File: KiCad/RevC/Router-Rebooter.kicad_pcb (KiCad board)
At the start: 2 copper layers, 62 x 49 mm, 18 parts, among them J1 12V Out, J3 12V In, K1 OMRON G5LE-1-VD, Q1 PN2222A, U1 PSU2-5, U2 ESP32-C3-Zero

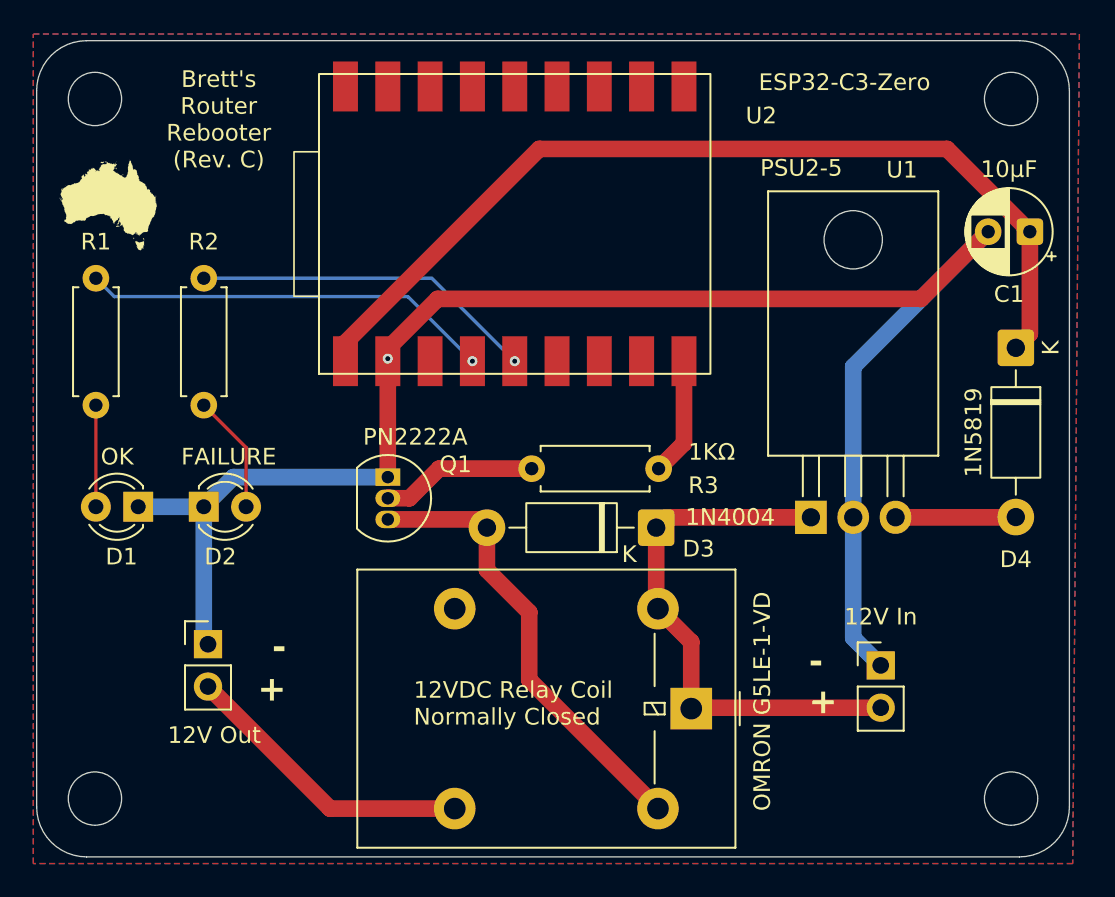
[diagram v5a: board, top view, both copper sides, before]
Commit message: Moved LED resistors to fix USB-C access to ESP32
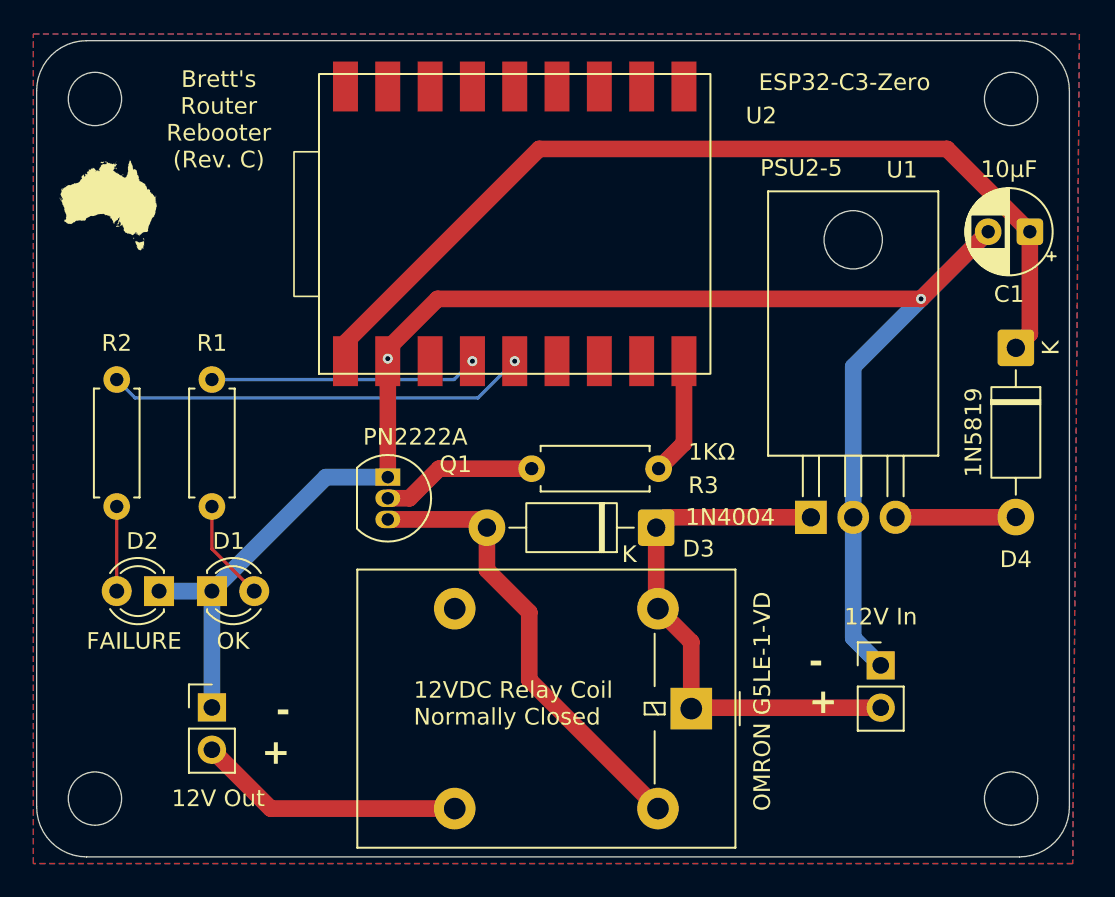
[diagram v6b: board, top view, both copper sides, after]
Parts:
- moved R1 9.25 mm to (67.8, 52.9)
- moved R2 8.02 mm to (62.1, 52.9)
- moved D1 6.73 mm to (67.8, 65.6), turned to 0 degrees
- moved D2 5.73 mm to (64.6, 65.6), turned to 180 degrees
- moved J1 3.80 mm to (67.8, 72.6)
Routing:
- net Net-(U2-IO0): track 24.7 -> 16.1 mm
- net Net-(U2-IO1): track 20.7 -> 25.3 mm
- net Net-(D2-A): track 7.15 -> 5.08 mm
- net /+12V_{OUT}: track 17.8 -> 16.0 mm
- net GND: track 100.8 -> 100.3 mm, vias 1 -> 2
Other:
- board text added: "Brett Hallen, Apr 2026"
- board text removed: "Brett Hallen, Mar 2026"
- board text removed: "USB Power Bypass Open: ESP32 powered via USB Closed: ESP32 powered via 12V input"
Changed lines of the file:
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@@
 	(title_block
 		(title "Broadband Router Rebooter")
-		(date "28/MAR/2026")
+		(date "30/APR/2026")
 		(rev "C")
 		(company "Brett Hallen")
@@
 	(footprint "Resistor_THT:R_Axial_DIN0207_L6.3mm_D2.5mm_P7.62mm_Horizontal"
 		(layer "F.Cu")
-		(at 60.8064 46.8524 -90)
+		(at 67.7734 52.9334 -90)
 		(descr "Resistor, Axial_DIN0207 series, Axial, Horizontal, pin pitch=7.62mm, 0.25W = 1/4W, length*diameter=6.3*2.5mm^2, http://cdn-reichelt.de/documents/datenblatt/B400/1_4W%23YAG.pdf")
 		(tags "Resistor Axial_DIN0207 series Axial Horizontal pin pitch 7.62mm 0.25W = 1/4W length 6.3mm diameter 2.5mm")
@@
 	(footprint "Connector_PinHeader_2.54mm:PinHeader_1x02_P2.54mm_Vertical"
 		(layer "F.Cu")
-		(at 67.5374 68.8234)
+		(at 67.7734 72.6184)
 		(descr "Through hole straight pin header, 1x02, 2.54mm pitch, single row")
 		(tags "Through hole pin header THT 1x02 2.54mm single row")
@@
 	(footprint "LED_THT:LED_D3.0mm"
 		(layer "F.Cu")
-		(at 67.2834 60.5684)
+		(at 64.5984 65.6334 180)
 		(descr "LED, diameter 3.0mm, 2 pins, generated by kicad-footprint-generator")
 		(tags "LED")
@@
 		)
 		(property "Sim.Pins" "1=K 2=A"
-			(at 0 0 0)
+			(at 0 0 180)
 			(unlocked yes)
 			(layer "F.Fab")
@@
 		(attr through_hole)
 		(fp_line
-			(start -0.29 -1.236)
-			(end -0.29 -1.08)
+			(start -0.29 1.08)
+			(end -0.29 1.236)
 			(stroke
 				(width 0.12)
@@
 		)
 		(fp_line
-			(start -0.29 1.08)
-			(end -0.29 1.236)
+			(start -0.29 -1.236)
+			(end -0.29 -1.08)
 			(stroke
 				(width 0.12)
@@
 		)
 		(fp_arc
-			(start -0.29 -1.235516)
-			(mid 1.36566 -1.987699)
-			(end 2.941437 -1.08)
+			(start 2.941437 1.08)
+			(mid 1.36566 1.987699)
+			(end -0.29 1.235516)
 			(stroke
 				(width 0.12)
@@
 		)
 		(fp_arc
-			(start 0.229039 -1.08)
-			(mid 1.27 -1.5)
-			(end 2.310961 -1.08)
+			(start 2.310961 1.08)
+			(mid 1.27 1.5)
+			(end 0.229039 1.08)
 			(stroke
 				(width 0.12)
@@
 		)
 		(fp_arc
-			(start 2.310961 1.08)
-			(mid 1.27 1.5)
-			(end 0.229039 1.08)
+			(start 0.229039 -1.08)
+			(mid 1.27 -1.5)
+			(end 2.310961 -1.08)
 			(stroke
 				(width 0.12)
@@
 		)
 		(fp_arc
-			(start 2.941437 1.08)
-			(mid 1.36566 1.987699)
-			(end -0.29 1.235516)
+			(start -0.29 -1.235516)
+			(mid 1.36566 -1.987699)
+			(end 2.941437 -1.08)
 			(stroke
 				(width 0.12)
@@
 		)
 		(fp_line
-			(start -1.15 -2.21)
-			(end -1.15 2.21)
+			(start 3.69 2.21)
+			(end 3.69 -2.21)
 			(stroke
 				(width 0.05)
@@
 		)
 		(fp_line
-			(start -1.15 2.21)
-			(end 3.69 2.21)
+			(start 3.69 -2.21)
+			(end -1.15 -2.21)
 			(stroke
 				(width 0.05)
@@
 		)
 		(fp_line
-			(start 3.69 -2.21)
-			(end -1.15 -2.21)
+			(start -1.15 2.21)
+			(end 3.69 2.21)
 			(stroke
 				(width 0.05)
@@
 		)
 		(fp_line
-			(start 3.69 2.21)
-			(end 3.69 -2.21)
+			(start -1.15 -2.21)
+			(end -1.15 2.21)
 			(stroke
 				(width 0.05)
@@
 		)
 		(pad "1" thru_hole rect
-			(at 0 0)
+			(at 0 0 180)
 			(size 1.8 1.8)
 			(drill 0.9)
@@
 		)
 		(pad "2" thru_hole circle
-			(at 2.54 0)
+			(at 2.54 0 180)
 			(size 1.8 1.8)
 			(drill 0.9)
@@
 	(footprint "LED_THT:LED_D3.0mm"
 		(layer "F.Cu")
-		(at 63.3464 60.5684 180)
+		(at 67.7734 65.6334)
 		(descr "LED, diameter 3.0mm, 2 pins, generated by kicad-footprint-generator")
 		(tags "LED")
@@
 		)
 		(property "Sim.Pins" "1=K 2=A"
-			(at 0 0 180)
+			(at 0 0 0)
 			(unlocked yes)
 			(layer "F.Fab")
@@
 		(attr through_hole)
 		(fp_line
-			(start -0.29 1.08)
-			(end -0.29 1.236)
+			(start -0.29 -1.236)
+			(end -0.29 -1.08)
 			(stroke
 				(width 0.12)
@@
 		)
 		(fp_line
-			(start -0.29 -1.236)
-			(end -0.29 -1.08)
+			(start -0.29 1.08)
+			(end -0.29 1.236)
 			(stroke
 				(width 0.12)
@@
 		)
 		(fp_arc
-			(start 2.941437 1.08)
-			(mid 1.36566 1.987699)
-			(end -0.29 1.235516)
+			(start -0.29 -1.235516)
+			(mid 1.36566 -1.987699)
+			(end 2.941437 -1.08)
 			(stroke
 				(width 0.12)
@@
 		)
 		(fp_arc
-			(start 2.310961 1.08)
-			(mid 1.27 1.5)
-			(end 0.229039 1.08)
+			(start 0.229039 -1.08)
+			(mid 1.27 -1.5)
+			(end 2.310961 -1.08)
 			(stroke
 				(width 0.12)
@@
 		)
 		(fp_arc
-			(start 0.229039 -1.08)
-			(mid 1.27 -1.5)
-			(end 2.310961 -1.08)
+			(start 2.310961 1.08)
+			(mid 1.27 1.5)
+			(end 0.229039 1.08)
 			(stroke
 				(width 0.12)
@@
 		)
 		(fp_arc
-			(start -0.29 -1.235516)
-			(mid 1.36566 -1.987699)
-			(end 2.941437 -1.08)
+			(start 2.941437 1.08)
+			(mid 1.36566 1.987699)
+			(end -0.29 1.235516)
 			(stroke
 				(width 0.12)
@@
 		)
 		(fp_line
-			(start 3.69 2.21)
-			(end 3.69 -2.21)
+			(start -1.15 -2.21)
+			(end -1.15 2.21)
 			(stroke
 				(width 0.05)
@@
 		)
 		(fp_line
-			(start 3.69 -2.21)
-			(end -1.15 -2.21)
+			(start -1.15 2.21)
+			(end 3.69 2.21)
 			(stroke
 				(width 0.05)
@@
 		)
 		(fp_line
-			(start -1.15 2.21)
-			(end 3.69 2.21)
+			(start 3.69 -2.21)
+			(end -1.15 -2.21)
 			(stroke
 				(width 0.05)
@@
 		)
 		(fp_line
-			(start -1.15 -2.21)
-			(end -1.15 2.21)
+			(start 3.69 2.21)
+			(end 3.69 -2.21)
 			(stroke
 				(width 0.05)
@@
 		)
 		(pad "1" thru_hole rect
-			(at 0 0 180)
+			(at 0 0)
 			(size 1.8 1.8)
 			(drill 0.9)
@@
 		)
 		(pad "2" thru_hole circle
-			(at 2.54 0 180)
+			(at 2.54 0)
 			(size 1.8 1.8)
 			(drill 0.9)
@@
 	(footprint "Resistor_THT:R_Axial_DIN0207_L6.3mm_D2.5mm_P7.62mm_Horizontal"
 		(layer "F.Cu")
-		(at 67.2834 46.8524 -90)
+		(at 62.0584 52.9334 -90)
 		(descr "Resistor, Axial_DIN0207 series, Axial, Horizontal, pin pitch=7.62mm, 0.25W = 1/4W, length*diameter=6.3*2.5mm^2, http://cdn-reichelt.de/documents/datenblatt/B400/1_4W%23YAG.pdf")
 		(tags "Resistor Axial_DIN0207 series Axial Horizontal pin pitch 7.62mm 0.25W = 1/4W length 6.3mm diameter 2.5mm")
@@
 	)
 	(gr_text "+\n-"
-		(at 72.2364 68.3154 180)
+		(at 72.4724 72.1104 180)
 		(layer "F.SilkS")
 		(effects
@@
 		)
 	)
-	(gr_text "Brett Hallen, Mar 2026"
+	(gr_text "Brett Hallen, Apr 2026"
 		(at 93.3834 44.0894 0)
 		(layer "B.SilkS")
@@
 		)
 	)
-	(gr_text "USB Power Bypass\nOpen:   ESP32 powered via USB\nClosed: ESP32 powered via 12V input"
-		(at 110.0824 67.1724 270)
-		(layer "B.SilkS")
-		(effects
-			(font
-				(size 1 1)
-				(thickness 0.1)
-			)
-			(justify left bottom mirror)
-		)
-	)
 	(gr_text "ESP32\nWiFi\nantenna\nzone\nLeave\nclear"
 		(at 94.4434 47.2184 0)
@@
 	)
 	(segment
-		(start 60.8064 54.4724)
-		(end 60.8064 60.5684)
+		(start 67.7734 60.5534)
+		(end 67.7734 63.0934)
+		(width 0.2)
+		(layer "F.Cu")
+		(net 1)
+	)
+	(segment
+		(start 67.7734 63.0934)
+		(end 70.3134 65.6334)
 		(width 0.2)
 		(layer "F.Cu")
@@
 		(net 3)
 	)
+	(via
+		(at 110.343512 48.0904)
+		(size 0.6)
+		(drill 0.3)
+		(layers "F.Cu" "B.Cu")
+		(net 3)
+	)
 	(segment
-		(start 78.3324 58.7904)
-		(end 69.0614 58.7904)
+		(start 67.7734 65.6334)
+		(end 67.7734 72.6184)
 		(width 1)
 		(layer "B.Cu")
@@
 	)
 	(segment
-		(start 69.0614 58.7904)
-		(end 67.2834 60.5684)
+		(start 78.3324 58.7904)
+		(end 74.6164 58.7904)
 		(width 1)
 		(layer "B.Cu")
@@
 	)
 	(segment
-		(start 67.2834 60.5684)
-		(end 63.3464 60.5684)
+		(start 67.7734 65.6334)
+		(end 64.5984 65.6334)
 		(width 1)
 		(layer "B.Cu")
@@
 	)
 	(segment
-		(start 67.2834 60.5684)
-		(end 67.2834 68.5694)
+		(start 110.343512 48.0904)
+		(end 114.375512 44.0584)
 		(width 1)
 		(layer "B.Cu")
@@
 	)
 	(segment
-		(start 67.2834 68.5694)
-		(end 67.5374 68.8234)
+		(start 74.6164 58.7904)
+		(end 67.7734 65.6334)
 		(width 1)
 		(layer "B.Cu")
@@
 	(segment
 		(start 106.2724 52.161512)
-		(end 114.375512 44.0584)
+		(end 110.343512 48.0904)
 		(width 1)
 		(layer "B.Cu")
@@
 	)
 	(segment
-		(start 82.3504 78.6894)
-		(end 74.8634 78.6894)
+		(start 71.3044 78.6894)
+		(end 67.7734 75.1584)
 		(width 1)
 		(layer "F.Cu")
@@
 	)
 	(segment
-		(start 74.8634 78.6894)
-		(end 67.5374 71.3634)
+		(start 82.3504 78.6894)
+		(end 71.3044 78.6894)
 		(width 1)
 		(layer "F.Cu")
@@
 	)
 	(segment
-		(start 69.8234 57.0124)
-		(end 67.2834 54.4724)
-		(width 0.2)
-		(layer "F.Cu")
-		(net 6)
-	)
-	(segment
-		(start 69.8234 60.5684)
-		(end 69.8234 57.0124)
+		(start 62.0584 60.5534)
+		(end 62.0584 65.6334)
 		(width 0.2)
 		(layer "F.Cu")
@@
 	)
 	(segment
-		(start 83.4104 51.8294)
-		(end 79.5344 47.9534)
-		(width 0.2)
-		(layer "B.Cu")
-		(net 11)
-	)
-	(segment
-		(start 79.5344 47.9534)
-		(end 61.9074 47.9534)
+		(start 67.7734 52.9334)
+		(end 82.3064 52.9334)
 		(width 0.2)
 		(layer "B.Cu")
@@
 	)
 	(segment
-		(start 61.9074 47.9534)
-		(end 60.8064 46.8524)
+		(start 82.3064 52.9334)
+		(end 83.4104 51.8294)
 		(width 0.2)
 		(layer "B.Cu")
@@
 	)
 	(segment
-		(start 80.9734 46.8524)
-		(end 67.2834 46.8524)
+		(start 83.7454 54.0344)
+		(end 85.9504 51.8294)
+		(width 0.2)
+		(layer "B.Cu")
+		(net 12)
+	)
+	(segment
+		(start 63.1594 54.0344)
+		(end 83.7454 54.0344)
 		(width 0.2)
 		(layer "B.Cu")
@@
 	)
 	(segment
-		(start 85.9504 51.8294)
-		(end 80.9734 46.8524)
+		(start 62.0584 52.9334)
+		(end 63.1594 54.0344)
 		(width 0.2)
 		(layer "B.Cu")
